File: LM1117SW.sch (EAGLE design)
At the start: 18 parts

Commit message: updated schematics with step down vreg
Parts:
- removed +, 12, 12V, 13, 14, GND: LSP10, solpad:LSP10
- removed C5, C6: 10uF, rcl:C-EUC0805K
- removed JMP1: 0R-JUMPC, jump-0r-smd:0R-JUMPC
- removed MDL1: (no value), ESP8266-ESP12E:ESP8266-12EESP8266-ESP12E
- removed R3: 100k, rcl:R-EU_R0603
- removed R4: 10k, rcl:R-EU_R0603
- removed R5, R6: (no value), rcl:R-EU_R0402
- removed U$3: (no value), Fabian:3-WIRE_CONNWIRE
- added C1, C2: 10uF, rcl:C-EUC0805K
- added R1: (no value), rcl:R-EU_R0402
- added U$1: LM1117, Fabian:LM1117
- R2: value 0R -> (none); device rcl:R-EU_R0805 -> rcl:R-EU_R0402; MF BOURNS -> (none); MPN CR0603-J/-000ELF -> (none); OC_FARNELL 2467553 -> (none)
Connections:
- removed net +12V: +.MP, 12V.MP, R3.2, U$2.VIN
- removed net N$1 (its old number): 13.MP
- removed net N$10: MDL1.ADC, R3.1, R4.2
- removed net N$11: JMP1-0R.1, MDL1.REST
- removed net N$12: JMP1-0R.2, MDL1.CH_PD
- removed net N$15: R5.2, R6.1, U$2.VSENSE
- removed net N$5: 14.MP
- removed net N$6: MDL1.GPIO13
- removed net N$7: MDL1.TXD, U$3.SIG
- removed net N$8: MDL1.RXD, U$3.5V
- removed net N$9: MDL1.GPIO0, R2.1
- removed net VCC: C5.1, C6.1, JMP1-0R.3, L1.P$2, MDL1.VCC, R5.1
- net GND: now also C1.2, C2.2, U$1.GND; no longer C5.2, C6.2, GND.MP, MDL1.GND, MDL1.GPIO15, R4.1, R6.2, U$3.0V
- net N$2: now also C1.1, C2.1, L1.P$2, R1.1, U$1.OUT; no longer MDL1.GPIO14
- net N$3: now also R1.2, R2.1, U$2.VSENSE; no longer MDL1.GPIO12
- net N$4: now also U$1.IN, U$2.VIN; no longer 12.MP
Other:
- moved on the sheet: L1, R2, U$2

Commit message: layout stuff
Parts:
- R1, R2: device rcl:R-EU_R0402 -> rcl:R-EU_R0603
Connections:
- net N$2 renamed VOUT
- net N$3 renamed SENS
- net N$4 renamed VIN
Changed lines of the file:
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@@
 <grid distance="0.1" unitdist="inch" unit="inch" style="lines" multiple="1" display="no" altdistance="0.01" altunitdist="inch" altunit="inch"/>
 <layers>
-<layer number="1" name="Top" color="4" fill="1" visible="no" active="no"/>
-<layer number="2" name="Route2" color="1" fill="3" visible="no" active="no"/>
-<layer number="3" name="Route3" color="4" fill="3" visible="no" active="no"/>
-<layer number="14" name="Route14" color="1" fill="6" visible="no" active="no"/>
-<layer number="15" name="Route15" color="4" fill="6" visible="no" active="no"/>
-<layer number="16" name="Bottom" color="1" fill="1" visible="no" active="no"/>
-<layer number="17" name="Pads" color="2" fill="1" visible="no" active="no"/>
-<layer number="18" name="Vias" color="2" fill="1" visible="no" active="no"/>
-<layer number="19" name="Unrouted" color="6" fill="1" visible="no" active="no"/>
-<layer number="20" name="Dimension" color="15" fill="1" visible="no" active="no"/>
-<layer number="21" name="tPlace" color="7" fill="1" visible="no" active="no"/>
-<layer number="22" name="bPlace" color="7" fill="1" visible="no" active="no"/>
-<layer number="23" name="tOrigins" color="15" fill="1" visible="no" active="no"/>
-<layer number="24" name="bOrigins" color="15" fill="1" visible="no" active="no"/>
-<layer number="25" name="tNames" color="7" fill="1" visible="no" active="no"/>
-<layer number="26" name="bNames" color="7" fill="1" visible="no" active="no"/>
-<layer number="27" name="tValues" color="7" fill="1" visible="no" active="no"/>
-<layer number="28" name="bValues" color="7" fill="1" visible="no" active="no"/>
+<layer number="1" name="Top" color="4" fill="1" visible="yes" active="no"/>
+<layer number="2" name="Route2" color="1" fill="3" visible="yes" active="no"/>
+<layer number="3" name="Route3" color="4" fill="3" visible="yes" active="no"/>
+<layer number="14" name="Route14" color="1" fill="6" visible="yes" active="no"/>
+<layer number="15" name="Route15" color="4" fill="6" visible="yes" active="no"/>
+<layer number="16" name="Bottom" color="1" fill="1" visible="yes" active="no"/>
+<layer number="17" name="Pads" color="2" fill="1" visible="yes" active="no"/>
+<layer number="18" name="Vias" color="2" fill="1" visible="yes" active="no"/>
+<layer number="19" name="Unrouted" color="6" fill="1" visible="yes" active="no"/>
+<layer number="20" name="Dimension" color="15" fill="1" visible="yes" active="no"/>
+<layer number="21" name="tPlace" color="7" fill="1" visible="yes" active="no"/>
+<layer number="22" name="bPlace" color="7" fill="1" visible="yes" active="no"/>
+<layer number="23" name="tOrigins" color="15" fill="1" visible="yes" active="no"/>
+<layer number="24" name="bOrigins" color="15" fill="1" visible="yes" active="no"/>
+<layer number="25" name="tNames" color="7" fill="1" visible="yes" active="no"/>
+<layer number="26" name="bNames" color="7" fill="1" visible="yes" active="no"/>
+<layer number="27" name="tValues" color="7" fill="1" visible="yes" active="no"/>
+<layer number="28" name="bValues" color="7" fill="1" visible="yes" active="no"/>
 <layer number="29" name="tStop" color="7" fill="3" visible="no" active="no"/>
 <layer number="30" name="bStop" color="7" fill="6" visible="no" active="no"/>
@@
 <layer number="35" name="tGlue" color="7" fill="4" visible="no" active="no"/>
 <layer number="36" name="bGlue" color="7" fill="5" visible="no" active="no"/>
-<layer number="37" name="tTest" color="7" fill="1" visible="no" active="no"/>
-<layer number="38" name="bTest" color="7" fill="1" visible="no" active="no"/>
+<layer number="37" name="tTest" color="7" fill="1" visible="yes" active="no"/>
+<layer number="38" name="bTest" color="7" fill="1" visible="yes" active="no"/>
 <layer number="39" name="tKeepout" color="4" fill="11" visible="no" active="no"/>
 <layer number="40" name="bKeepout" color="1" fill="11" visible="no" active="no"/>
@@
 <layer number="44" name="Drills" color="7" fill="1" visible="no" active="no"/>
 <layer number="45" name="Holes" color="7" fill="1" visible="no" active="no"/>
-<layer number="46" name="Milling" color="3" fill="1" visible="no" active="no"/>
-<layer number="47" name="Measures" color="7" fill="1" visible="no" active="no"/>
-<layer number="48" name="Document" color="7" fill="1" visible="no" active="no"/>
-<layer number="49" name="Reference" color="7" fill="1" visible="no" active="no"/>
-<layer number="51" name="tDocu" color="7" fill="1" visible="no" active="no"/>
-<layer number="52" name="bDocu" color="7" fill="1" visible="no" active="no"/>
+<layer number="46" name="Milling" color="3" fill="1" visible="yes" active="no"/>
+<layer number="47" name="Measures" color="7" fill="1" visible="yes" active="no"/>
+<layer number="48" name="Document" color="7" fill="1" visible="yes" active="no"/>
+<layer number="49" name="Reference" color="7" fill="1" visible="yes" active="no"/>
+<layer number="51" name="tDocu" color="7" fill="1" visible="yes" active="no"/>
+<layer number="52" name="bDocu" color="7" fill="1" visible="yes" active="no"/>
 <layer number="90" name="Modules" color="5" fill="1" visible="yes" active="yes"/>
 <layer number="91" name="Nets" color="2" fill="1" visible="yes" active="yes"/>
@@
 <class number="0" name="default" width="0" drill="0">
 </class>
+<class number="1" name="power" width="0.6096" drill="0">
+</class>
 </classes>
 <parts>
 <part name="L1" library="Fabian" deviceset="L_10UH_560MA" device=""/>
 <part name="U$2" library="Fabian" deviceset="TPS560200" device=""/>
-<part name="R1" library="rcl" deviceset="R-EU_" device="R0402"/>
-<part name="R2" library="rcl" deviceset="R-EU_" device="R0402"/>
+<part name="R1" library="rcl" deviceset="R-EU_" device="R0603"/>
+<part name="R2" library="rcl" deviceset="R-EU_" device="R0603"/>
 <part name="C1" library="rcl" deviceset="C-EU" device="C0805K" value="10uF">
 <attribute name="OC_FARNELL" value="1759421"/>
@@
 </busses>
 <nets>
-<net name="N$1" class="0">
+<net name="N$1" class="1">
 <segment>
 <pinref part="L1" gate="G$1" pin="P$1"/>
@@
 </segment>
 </net>
-<net name="N$2" class="0">
+<net name="VOUT" class="1">
 <segment>
 <pinref part="L1" gate="G$1" pin="P$2"/>
@@
 <wire x1="157.48" y1="25.4" x2="157.48" y2="66.04" width="0.1524" layer="91"/>
 <wire x1="157.48" y1="66.04" x2="139.7" y2="66.04" width="0.1524" layer="91"/>
+<label x="99.06" y="66.04" size="1.778" layer="95"/>
+<label x="55.88" y="25.4" size="1.778" layer="95"/>
 </segment>
 </net>
-<net name="N$3" class="0">
+<net name="SENS" class="0">
 <segment>
 <pinref part="R2" gate="G$1" pin="1"/>
@@
 <pinref part="U$2" gate="G$1" pin="VSENSE"/>
 <wire x1="17.78" y1="55.88" x2="22.86" y2="55.88" width="0.1524" layer="91"/>
+<label x="66.04" y="40.64" size="1.778" layer="95"/>
 </segment>
 </net>
-<net name="GND" class="0">
+<net name="GND" class="1">
 <segment>
 <pinref part="R2" gate="G$1" pin="2"/>
@@
 <wire x1="53.34" y1="55.88" x2="55.88" y2="55.88" width="0.1524" layer="91"/>
 <wire x1="55.88" y1="55.88" x2="55.88" y2="53.34" width="0.1524" layer="91"/>
+<label x="55.88" y="55.88" size="1.778" layer="95"/>
 </segment>
 <segment>
@@
 </segment>
 </net>
-<net name="N$4" class="0">
+<net name="VIN" class="1">
 <segment>
 <pinref part="U$2" gate="G$1" pin="VIN"/>
@@
 <pinref part="U$1" gate="G$1" pin="IN"/>
 <wire x1="7.62" y1="25.4" x2="20.32" y2="25.4" width="0.1524" layer="91"/>
+<label x="12.7" y="66.04" size="1.778" layer="95"/>
 </segment>
 </net>

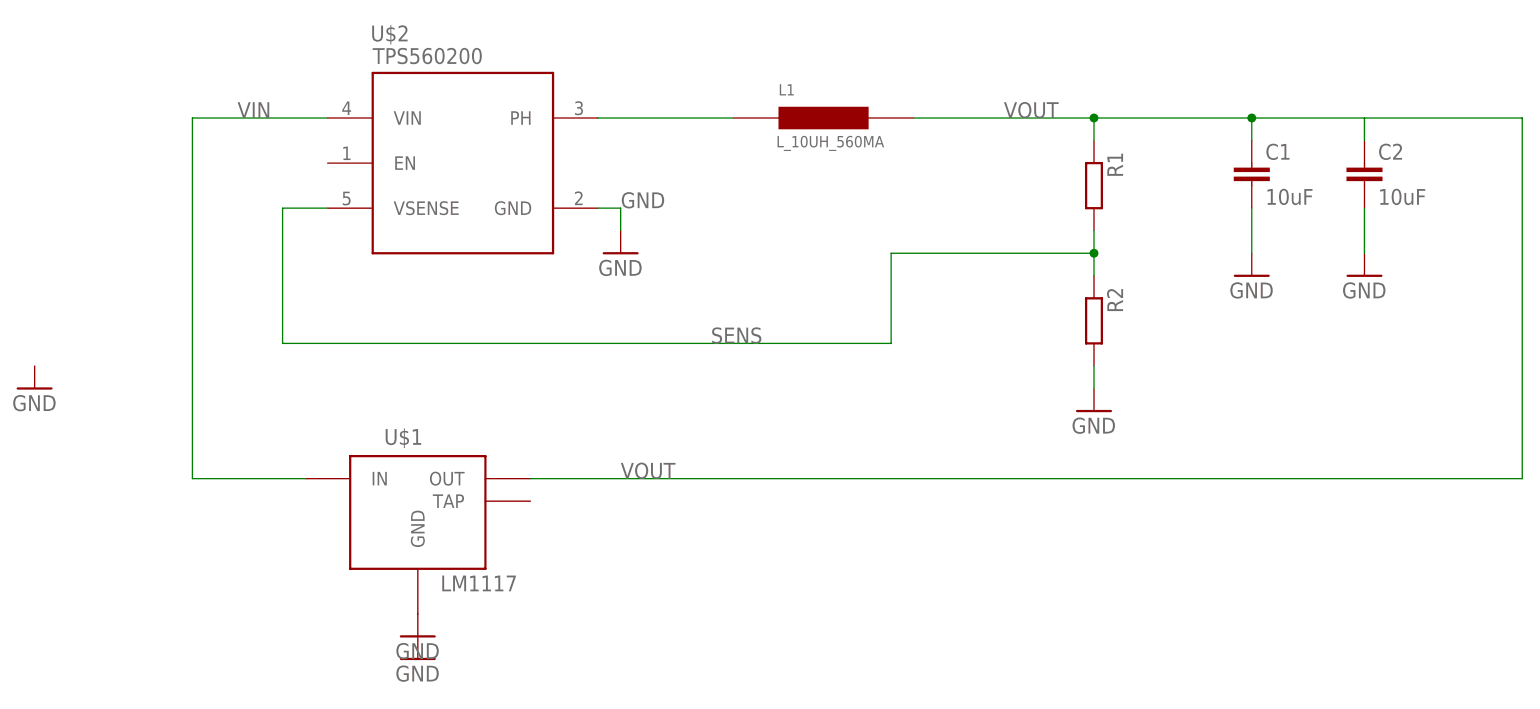
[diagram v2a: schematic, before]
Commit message: finished LM1117 replacement
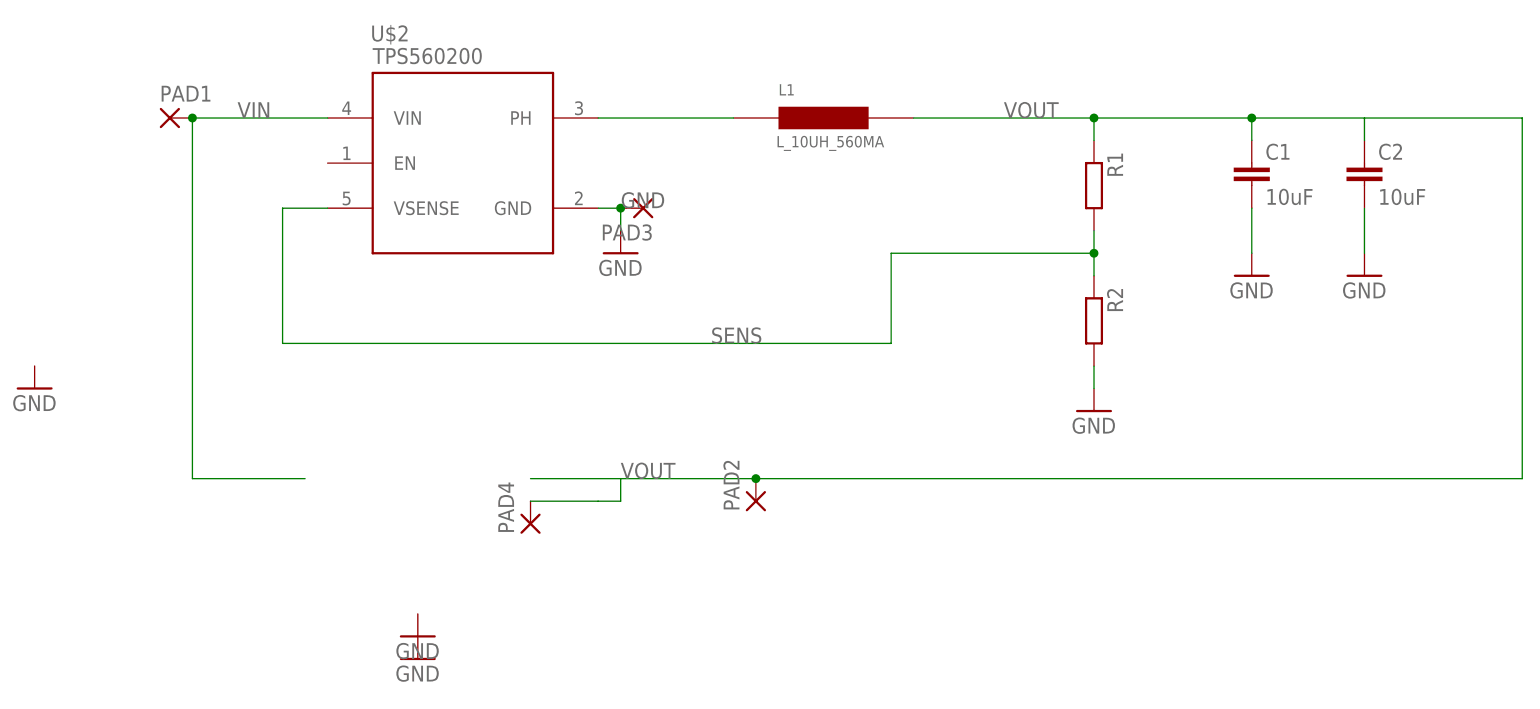
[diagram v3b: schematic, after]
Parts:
- removed U$1: LM1117, Fabian:LM1117
- added PAD1, PAD2, PAD3, PAD4: (no value), wirepad:1,6/0,9
- R1, R2: device rcl:R-EU_R0603 -> rcl:R-EU_R0402
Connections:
- net GND: now also PAD3.P; no longer U$1.GND
- net VIN: now also PAD1.P; no longer U$1.IN
- net VOUT: now also PAD2.P, PAD4.P; no longer U$1.OUT
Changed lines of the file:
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@@
 <grid distance="0.1" unitdist="inch" unit="inch" style="lines" multiple="1" display="no" altdistance="0.01" altunitdist="inch" altunit="inch"/>
 <layers>
-<layer number="1" name="Top" color="4" fill="1" visible="yes" active="no"/>
-<layer number="2" name="Route2" color="1" fill="3" visible="yes" active="no"/>
-<layer number="3" name="Route3" color="4" fill="3" visible="yes" active="no"/>
-<layer number="14" name="Route14" color="1" fill="6" visible="yes" active="no"/>
-<layer number="15" name="Route15" color="4" fill="6" visible="yes" active="no"/>
-<layer number="16" name="Bottom" color="1" fill="1" visible="yes" active="no"/>
-<layer number="17" name="Pads" color="2" fill="1" visible="yes" active="no"/>
-<layer number="18" name="Vias" color="2" fill="1" visible="yes" active="no"/>
-<layer number="19" name="Unrouted" color="6" fill="1" visible="yes" active="no"/>
-<layer number="20" name="Dimension" color="15" fill="1" visible="yes" active="no"/>
-<layer number="21" name="tPlace" color="7" fill="1" visible="yes" active="no"/>
-<layer number="22" name="bPlace" color="7" fill="1" visible="yes" active="no"/>
-<layer number="23" name="tOrigins" color="15" fill="1" visible="yes" active="no"/>
-<layer number="24" name="bOrigins" color="15" fill="1" visible="yes" active="no"/>
-<layer number="25" name="tNames" color="7" fill="1" visible="yes" active="no"/>
-<layer number="26" name="bNames" color="7" fill="1" visible="yes" active="no"/>
-<layer number="27" name="tValues" color="7" fill="1" visible="yes" active="no"/>
-<layer number="28" name="bValues" color="7" fill="1" visible="yes" active="no"/>
+<layer number="1" name="Top" color="4" fill="1" visible="no" active="no"/>
+<layer number="2" name="Route2" color="1" fill="3" visible="no" active="no"/>
+<layer number="3" name="Route3" color="4" fill="3" visible="no" active="no"/>
+<layer number="14" name="Route14" color="1" fill="6" visible="no" active="no"/>
+<layer number="15" name="Route15" color="4" fill="6" visible="no" active="no"/>
+<layer number="16" name="Bottom" color="1" fill="1" visible="no" active="no"/>
+<layer number="17" name="Pads" color="2" fill="1" visible="no" active="no"/>
+<layer number="18" name="Vias" color="2" fill="1" visible="no" active="no"/>
+<layer number="19" name="Unrouted" color="6" fill="1" visible="no" active="no"/>
+<layer number="20" name="Dimension" color="15" fill="1" visible="no" active="no"/>
+<layer number="21" name="tPlace" color="7" fill="1" visible="no" active="no"/>
+<layer number="22" name="bPlace" color="7" fill="1" visible="no" active="no"/>
+<layer number="23" name="tOrigins" color="15" fill="1" visible="no" active="no"/>
+<layer number="24" name="bOrigins" color="15" fill="1" visible="no" active="no"/>
+<layer number="25" name="tNames" color="7" fill="1" visible="no" active="no"/>
+<layer number="26" name="bNames" color="7" fill="1" visible="no" active="no"/>
+<layer number="27" name="tValues" color="7" fill="1" visible="no" active="no"/>
+<layer number="28" name="bValues" color="7" fill="1" visible="no" active="no"/>
 <layer number="29" name="tStop" color="7" fill="3" visible="no" active="no"/>
 <layer number="30" name="bStop" color="7" fill="6" visible="no" active="no"/>
@@
 <layer number="35" name="tGlue" color="7" fill="4" visible="no" active="no"/>
 <layer number="36" name="bGlue" color="7" fill="5" visible="no" active="no"/>
-<layer number="37" name="tTest" color="7" fill="1" visible="yes" active="no"/>
-<layer number="38" name="bTest" color="7" fill="1" visible="yes" active="no"/>
+<layer number="37" name="tTest" color="7" fill="1" visible="no" active="no"/>
+<layer number="38" name="bTest" color="7" fill="1" visible="no" active="no"/>
 <layer number="39" name="tKeepout" color="4" fill="11" visible="no" active="no"/>
 <layer number="40" name="bKeepout" color="1" fill="11" visible="no" active="no"/>
@@
 <layer number="44" name="Drills" color="7" fill="1" visible="no" active="no"/>
 <layer number="45" name="Holes" color="7" fill="1" visible="no" active="no"/>
-<layer number="46" name="Milling" color="3" fill="1" visible="yes" active="no"/>
-<layer number="47" name="Measures" color="7" fill="1" visible="yes" active="no"/>
-<layer number="48" name="Document" color="7" fill="1" visible="yes" active="no"/>
-<layer number="49" name="Reference" color="7" fill="1" visible="yes" active="no"/>
-<layer number="51" name="tDocu" color="7" fill="1" visible="yes" active="no"/>
-<layer number="52" name="bDocu" color="7" fill="1" visible="yes" active="no"/>
+<layer number="46" name="Milling" color="3" fill="1" visible="no" active="no"/>
+<layer number="47" name="Measures" color="7" fill="1" visible="no" active="no"/>
+<layer number="48" name="Document" color="7" fill="1" visible="no" active="no"/>
+<layer number="49" name="Reference" color="7" fill="1" visible="no" active="no"/>
+<layer number="51" name="tDocu" color="7" fill="1" visible="no" active="no"/>
+<layer number="52" name="bDocu" color="7" fill="1" visible="no" active="no"/>
 <layer number="90" name="Modules" color="5" fill="1" visible="yes" active="yes"/>
 <layer number="91" name="Nets" color="2" fill="1" visible="yes" active="yes"/>
@@
 <part name="L1" library="Fabian" deviceset="L_10UH_560MA" device=""/>
 <part name="U$2" library="Fabian" deviceset="TPS560200" device=""/>
-<part name="R1" library="rcl" deviceset="R-EU_" device="R0603"/>
-<part name="R2" library="rcl" deviceset="R-EU_" device="R0603"/>
+<part name="R1" library="rcl" deviceset="R-EU_" device="R0402"/>
+<part name="R2" library="rcl" deviceset="R-EU_" device="R0402"/>
 <part name="C1" library="rcl" deviceset="C-EU" device="C0805K" value="10uF">
 <attribute name="OC_FARNELL" value="1759421"/>
@@
 <part name="GND4" library="supply1" deviceset="GND" device=""/>
 <part name="GND5" library="supply1" deviceset="GND" device=""/>
-<part name="U$1" library="Fabian" deviceset="LM1117" device=""/>
 <part name="GND6" library="supply1" deviceset="GND" device=""/>
 <part name="GND7" library="supply1" deviceset="GND" device=""/>
+<part name="PAD1" library="wirepad" deviceset="1,6/0,9" device=""/>
+<part name="PAD2" library="wirepad" deviceset="1,6/0,9" device=""/>
+<part name="PAD3" library="wirepad" deviceset="1,6/0,9" device=""/>
+<part name="PAD4" library="wirepad" deviceset="1,6/0,9" device=""/>
 </parts>
 <sheets>
@@
 <instance part="GND4" gate="1" x="139.7" y="48.26"/>
 <instance part="GND5" gate="1" x="-10.16" y="35.56"/>
-<instance part="U$1" gate="G$1" x="33.02" y="22.86"/>
 <instance part="GND6" gate="1" x="33.02" y="5.08"/>
 <instance part="GND7" gate="1" x="33.02" y="7.62"/>
+<instance part="PAD1" gate="1" x="5.08" y="66.04"/>
+<instance part="PAD2" gate="1" x="71.12" y="22.86" rot="R90"/>
+<instance part="PAD3" gate="1" x="58.42" y="55.88" rot="R180"/>
+<instance part="PAD4" gate="1" x="45.72" y="20.32" rot="R90"/>
 </instances>
 <busses>
@@
 <junction x="109.22" y="66.04"/>
 <junction x="127" y="66.04"/>
-<pinref part="U$1" gate="G$1" pin="OUT"/>
-<wire x1="45.72" y1="25.4" x2="157.48" y2="25.4" width="0.1524" layer="91"/>
+<wire x1="45.72" y1="25.4" x2="55.88" y2="25.4" width="0.1524" layer="91"/>
+<wire x1="55.88" y1="25.4" x2="71.12" y2="25.4" width="0.1524" layer="91"/>
+<wire x1="71.12" y1="25.4" x2="157.48" y2="25.4" width="0.1524" layer="91"/>
 <wire x1="157.48" y1="25.4" x2="157.48" y2="66.04" width="0.1524" layer="91"/>
 <wire x1="157.48" y1="66.04" x2="139.7" y2="66.04" width="0.1524" layer="91"/>
 <label x="99.06" y="66.04" size="1.778" layer="95"/>
 <label x="55.88" y="25.4" size="1.778" layer="95"/>
+<pinref part="PAD2" gate="1" pin="P"/>
+<junction x="71.12" y="25.4"/>
+<pinref part="PAD4" gate="1" pin="P"/>
+<wire x1="45.72" y1="22.86" x2="53.34" y2="22.86" width="0.1524" layer="91"/>
+<wire x1="53.34" y1="22.86" x2="55.88" y2="22.86" width="0.1524" layer="91"/>
+<wire x1="55.88" y1="22.86" x2="55.88" y2="25.4" width="0.1524" layer="91"/>
 </segment>
 </net>
@@
 <wire x1="55.88" y1="55.88" x2="55.88" y2="53.34" width="0.1524" layer="91"/>
 <label x="55.88" y="55.88" size="1.778" layer="95"/>
-</segment>
-<segment>
-<pinref part="U$1" gate="G$1" pin="GND"/>
-<pinref part="GND7" gate="1" pin="GND"/>
+<pinref part="PAD3" gate="1" pin="P"/>
+<junction x="55.88" y="55.88"/>
 </segment>
 </net>
@@
 <wire x1="22.86" y1="66.04" x2="7.62" y2="66.04" width="0.1524" layer="91"/>
 <wire x1="7.62" y1="66.04" x2="7.62" y2="25.4" width="0.1524" layer="91"/>
-<pinref part="U$1" gate="G$1" pin="IN"/>
 <wire x1="7.62" y1="25.4" x2="20.32" y2="25.4" width="0.1524" layer="91"/>
 <label x="12.7" y="66.04" size="1.778" layer="95"/>
-</segment>
-</net>
+<pinref part="PAD1" gate="1" pin="P"/>
+<junction x="7.62" y="66.04"/>
+</segment>
+</net>
